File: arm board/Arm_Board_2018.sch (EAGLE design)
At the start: 212 parts, among them J1 RJ45KEYSTONE-942, J10 APP_2POS_CONFIGGENERAL_CONFIG, J11 APP_2POS_CONFIGGENERAL_CONFIG, J12 APP_2POS_CONFIGGENERAL_CONFIG, J13 APP_2POS_CONFIGGENERAL_CONFIG, J14 SL02, J15 SL02, J16 SL02, J2 JTAG_ARM_10PIN, J4 SL02, J5 APP_2POS_CONFIGGENERAL_CONFIG, J6 APP_2POS_CONFIGGENERAL_CONFIG, J7 APP_2POS_CONFIGGENERAL_CONFIG, J9 APP_2POS_CONFIGGENERAL_CONFIG, Q1 Q_IRF7437SMD, U1 TM4C1294NCPDT, U2 HX1198FNL, U3 SLVU2.8-4, Y1 NX3225GA, Y2 CRYATL_32K_SMD

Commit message: Attached most of the powerlines
All major components put on the board. Most powerlines have been run.
Started to route a logic bus.
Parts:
- removed R60, R67, R68, R69, R70: 1k, SparkFun-Passives:RESISTOR0402-RES
- C50: device SparkFun-Capacitors:CAP1206 -> SparkFun-Passives:CAP0603-CAP
- C51: value 2.2uF -> 10nF; device SparkFun-Capacitors:CAP1206 -> SparkFun-Passives:CAP0603-CAP
- C61: value .1uF -> 2.2uF; device SparkFun-Passives:CAP0603-CAP -> SparkFun-Passives:CAP1206
- C62: value 1nF -> 2.2uF; device SparkFun-Passives:CAP0603-CAP -> SparkFun-Passives:CAP1206
- C63, C65, C67: value .1uF -> 0.1uF
- C64, C66, C68: value .1uF -> 10nF
- C69, C71, C73, C74: value 1uF -> 0.1uF
- C70, C72: value 1uF -> 10nF
- C75: value 2.2uF -> 1nF; device SparkFun-Capacitors:CAP1206 -> SparkFun-Passives:CAP0603-CAP
- R59: value 1k -> 1K
- U$21, U$22, U$23, U$24, U$25: value ACS781 -> ACS722LL; device MRDT-ICs:ACS781 -> MRDT-ICs:ACS722LL
- renumbered GND97 to POWER_12V2
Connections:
- removed net N$13: R60.1, U$25.VOUT
- removed net N$14: C53.2, Q1.D, U$19.SENSE, U$19.V+, U$26.IP-
- removed net N$2: R30.2, R31.2, U$12.VREF
- removed net N$26: R35.2, R36.2, U$13.VREF
- removed net N$3: C55.2, R18.2, R20.1, U$14.I0, U$14.I1, U$14.I2, U$14.I3, U$14.I4, U$14.NSLEEP, U$14.V3P3OUT
- removed net N$4: R40.2, R41.2, U$15.VREF
- removed net N$44: R70.1, U$20.VOUT
- new net N$100: R59.2, U$20.VOUT
- new net N$48: C53.2, Q1.D, U$19.SENSE, U$19.V+, U$20.IP-
- new net N$52: C65.2, U$21.SEL, U$21.VCC
- new net N$76: C64.2, U$21.VIOUT
- new net N$78: C67.2, U$22.SEL, U$22.VCC
- new net N$82: C66.2, U$22.VIOUT
- new net N$83: C69.2, U$24.SEL, U$24.VCC
- new net N$84: C68.2, U$24.VIOUT
- new net N$85: C71.2, U$26.SEL, U$26.VCC
- new net N$86: C70.2, U$26.VIOUT
- new net N$87: C73.2, U$25.SEL, U$25.VCC
- new net N$96: C72.2, U$25.VIOUT
- new net N$98: C63.2, U$23.SEL, U$23.VCC
- new net N$99: C51.2, U$23.VIOUT
- net 12VMOTOR_POWER: now also U$26.IP+; no longer U$20.IP+
- net GND: now also C61.1, C74.2; no longer C51.1, C61.2, C63.1, C64.1, C65.1, C66.1, C67.1, C68.1, C69.2, C70.2, C71.1, C72.1, C73.1, C74.1
- net LOGIC_3.3V: now also C50.1, C63.1, C65.1, C67.1, C69.1, C71.1, C73.1, C74.1; no longer C61.1, C63.2, C64.2, C65.2, C66.2, C67.2, C68.2, C75.1, U$21.VCC, U$22.VCC, U$23.VCC, U$24.VCC, U$25.VCC, U$26.SEL, U$26.VCC
- net MAINLINE_CURRENT_SENSOR: now also C75.1, R59.1; no longer C62.2, U$26.VIOUT
- net MOTOR1_CURRENT_SENSOR: now also C64.1; no longer C74.2, R70.2
- net MOTOR1_POWER: now also U$21.IP-; no longer U$20.IP-
- net MOTOR2_CURRENT_SENSOR: now also C66.1; no longer C73.2, R69.2
- net MOTOR3_CURRENT_SENSOR: now also C51.1; no longer C72.2, R68.2
- net MOTOR3_POWER: now also U$23.IP-; no longer U$21.IP-
- net MOTOR4_CURRENT_SENSOR: now also C68.1; no longer C71.2, R67.2
- net MOTOR4_POWER: now also U$24.IP-; no longer U$23.IP-
- net MOTOR5_CURRENT_SENSOR: now also C72.1; no longer C69.1, R59.2
- net MOTOR5_POWER: now also U$25.IP-; no longer U$24.IP-
- net MOTOR6_CURRENT_SENSOR: no longer R60.2
- net MOTOR6_POWER: now also U$26.IP-; no longer U$25.IP-
- net N$1: now also C55.2, R18.2, R20.2, U$14.I0, U$14.I1, U$14.I2, U$14.I3, U$14.I4, U$14.NSLEEP, U$14.V3P3OUT; no longer R25.2, R26.2, U$11.VREF
- net N$12: now also R20.1, R21.2, U$14.VREF; no longer R59.1, U$24.VOUT
- net N$15: now also R35.1, R36.2, U$13.VREF; no longer C57.2, R24.2, R25.1, U$11.I0, U$11.I1, U$11.I2, U$11.I3, U$11.I4, U$11.NSLEEP, U$11.V3P3OUT
- net N$20: now also C57.2, R24.2, R25.2, U$11.I0, U$11.I1, U$11.I2, U$11.I3, U$11.I4, U$11.NSLEEP, U$11.V3P3OUT; no longer R67.1, U$23.VOUT
- net N$21: now also R45.1, R46.2, U$16.VREF; no longer C56.2, R29.2, R30.1, U$12.I0, U$12.I1, U$12.I2, U$12.I3, U$12.I4, U$12.NSLEEP, U$12.V3P3OUT
- net N$27: now also R40.1, R41.2, U$15.VREF; no longer C58.2, R34.2, R35.1, U$13.I0, U$13.I1, U$13.I2, U$13.I3, U$13.I4, U$13.NSLEEP, U$13.V3P3OUT
- net N$32: now also C59.2, R39.2, R40.2, U$15.I0, U$15.I1, U$15.I2, U$15.I3, U$15.I4, U$15.NSLEEP, U$15.V3P3OUT; no longer R68.1, U$21.VOUT
- net N$33: now also C60.2, R44.2, R45.2, U$16.I0, U$16.I1, U$16.I2, U$16.I3, U$16.I4, U$16.NSLEEP, U$16.V3P3OUT; no longer C59.2, R39.2, R40.1, U$15.I0, U$15.I1, U$15.I2, U$15.I3, U$15.I4, U$15.NSLEEP, U$15.V3P3OUT
- net N$38: now also C56.2, R29.2, R30.2, U$12.I0, U$12.I1, U$12.I2, U$12.I3, U$12.I4, U$12.NSLEEP, U$12.V3P3OUT; no longer R69.1, U$22.VOUT
- net N$39: now also C58.2, R34.2, R35.2, U$13.I0, U$13.I1, U$13.I2, U$13.I3, U$13.I4, U$13.NSLEEP, U$13.V3P3OUT; no longer C60.2, R44.2, R45.1, U$16.I0, U$16.I1, U$16.I2, U$16.I3, U$16.I4, U$16.NSLEEP, U$16.V3P3OUT
- net N$5: now also R30.1, R31.2, U$12.VREF; no longer R45.2, R46.2, U$16.VREF
- net N$6: now also R25.1, R26.2, U$11.VREF; no longer R20.2, R21.2, U$14.VREF
- net VCC_12V: now also C61.2, C62.2, U$20.IP+; no longer C50.1, C51.2, U$26.IP+
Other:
- note added: "BOARD LEDS"
- note added: "MAIN POWER LINE"
- note removed: "MAIN POWER INPUT"
- note removed: "MOTOR MANUAL CONTROL LEDS"
- moved on the sheet: C21, C23, C25, C26, C29, C30, C33, C34, C37, C38, C41, C42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

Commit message: Add all pins, finished Rev 1, Not board reviewed
Added all the pins that were missing. Finished routing all logic lines.
Made board slightly smaller.
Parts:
- removed C24, C25, C28, C29, C32, C33, C36, C37, C40, C41, C48, C49, C54: .1uF, SparkFun-Passives:CAP0603-CAP
- removed C26, C30, C34, C38, C42: 100uF, SparkFun-Passives:CAP1210
- removed C27, C31, C35, C39, C43: .01uF, SparkFun-Passives:CAP0603-CAP
- removed C55, C56, C57, C58, C59, C60: .47uF, SparkFun-Passives:CAP0603-CAP
- removed R21, R24, R26, R29, R31, R34, R36, R39, R41, R44, R46: 10K, SparkFun-Passives:RESISTOR0402-RES
- removed R22, R27, R32, R37, R42, R47: 40m, SparkFun-Passives:RESISTOR2512
- removed R23, R28, R33, R38, R43, R48: 1m, SparkFun-Passives:RESISTOR0402-RES
- removed R25, R30, R35, R40, R45: 22.6K, SparkFun-Passives:RESISTOR0402-RES
- removed U$13, U$14, U$15, U$16: DRV8829, MRDT-ICs:DRV8829
- removed U$18, U$27, U$28: 74LVC1G3157, MRDT-ICs:74LVC1G3157
- added C76, C78, C80, C82: .1uF, SparkFun-Passives:CAP0603-CAP
- added C77, C79, C81, C83: 100uF, SparkFun-Passives:CAP1210
- added GROUND: APPPP45_PCB_HORIZ_RIGHT, MRDT-Connectors:APPPP45_PCB_HORIZ_RIGHT
- added OE_PULLUP, R60, R67, R68, R69: 10K, SparkFun-Passives:RESISTOR0402-RES
- added SCL_PULLUP, SDA_PULLUP: 1K, SparkFun-Passives:RESISTOR0402-RES
- added U$31, U$32, U$33, U$34: BTM7752G, MRDT-ICs:BTM7752G
- added U4: (no value), adafruit:PCA9685
- C21: value .1uF -> 100uF; device SparkFun-Passives:CAP0603-CAP -> SparkFun-Passives:CAP1210
- C22: value .01uF -> .1uF
- D1: value (none) -> J1
- D2: value (none) -> J2
- D3: value (none) -> J3
- D4: value (none) -> J4
- D5: value (none) -> J5
- D6: value (none) -> J6
- R20: value 22.6K -> 10K
- U$11, U$12: value DRV8829 -> BTM7752G; device MRDT-ICs:DRV8829 -> MRDT-ICs:BTM7752G
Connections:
- removed net MOTOR1_DEMUX_SEL: U$27.Z, U1G$1.PD3@4
- removed net MOTOR1_GEN0: U$27.S, U1G$1.PF1@43
- removed net MOTOR2_GEN1: U$14.ENABLE, U1G$1.PF2@44
- removed net MOTOR2_NFAULT: R18.1, U$14.NFAULT, U1G$1.PE0@15
- removed net MOTOR2_NRESET: U$14.NRESET, U1G$1.PE1@14
- removed net MOTOR2_PHASE: U$14.PHASE, U1G$1.PE2@13
- removed net MOTOR3_DEMUX_SEL: U$18.Z, U1G$1.PD5@126
- removed net MOTOR3_GEN1: U$18.S, U1G$1.PF3@45
- removed net MOTOR4_GEN2: U$11.ENABLE, U1G$1.PG0@49
- removed net MOTOR4_NFAULT: R24.1, U$11.NFAULT, U1G$1.PE3@12
- removed net MOTOR4_NRESET: U$11.NRESET, U1G$1.PE4@123
- removed net MOTOR4_PHASE: U$11.PHASE, U1G$1.PE5@124
- removed net MOTOR5_GEN2: U$12.ENABLE, U1G$1.PG1@50
- removed net MOTOR5_NFAULT: R29.1, U$12.NFAULT, U1G$1.PC4@25
- removed net MOTOR5_NRESET: U$12.NRESET, U1G$1.PC5@24
- removed net MOTOR5_PHASE: U$12.PHASE, U1G$1.PC6@23
- removed net MOTOR6_GEN3: U$13.ENABLE, U1G$1.PK4@63
- removed net MOTOR6_NFAULT: R34.1, U$13.NFAULT, U1G$1.PN2@109
- removed net MOTOR6_NRESET: U$13.NRESET, U1G$1.PN3@110
- removed net MOTOR6_PHASE: U$13.PHASE, U1G$1.PN4@111
- removed net MOTOR7/8_DEMUX_SEL: U$28.Z, U1G$1.PD7@128
- removed net MOTOR7/8_GEN3: U$28.S, U1G$1.PK5@62
- removed net MOTOR7_NFAULT: R39.1, U$15.NFAULT, U1G$1.PQ1@6
- removed net MOTOR7_NRESET: U$15.NRESET, U1G$1.PQ2@11
- removed net MOTOR7_PHASE: U$15.PHASE, U1G$1.PQ3@27
- removed net MOTOR7_PWM: U$15.ENABLE, U$28.Y1
- removed net MOTOR8_NFAULT: R44.1, U$16.NFAULT, U1G$1.PQ0@5
- removed net MOTOR8_NRESET: U$16.NRESET, U1G$1.PP0@118
- removed net MOTOR8_PHASE: U$16.PHASE, U1G$1.PP1@119
- removed net MOTOR8_PWM: U$16.ENABLE, U$28.Y0
- removed net N$1: C55.2, R18.2, R20.2, U$14.I0, U$14.I1, U$14.I2, U$14.I3, U$14.I4, U$14.NSLEEP, U$14.V3P3OUT
- removed net N$10: C22.1, U$14.CP1
- removed net N$11: C22.2, U$14.CP2
- removed net N$12: R20.1, R21.2, U$14.VREF
- removed net N$15: R35.1, R36.2, U$13.VREF
- removed net N$16: R27.1, U$11.ISENSE
- removed net N$17: C24.1, R28.1, U$11.VCP
- removed net N$18: C27.1, U$11.CP1
- removed net N$19: C27.2, U$11.CP2
- removed net N$20: C57.2, R24.2, R25.2, U$11.I0, U$11.I1, U$11.I2, U$11.I3, U$11.I4, U$11.NSLEEP, U$11.V3P3OUT
- removed net N$21: R45.1, R46.2, U$16.VREF
- removed net N$22: R32.1, U$12.ISENSE
- removed net N$23: C28.1, R33.1, U$12.VCP
- removed net N$24: C31.1, U$12.CP1
- removed net N$25: C31.2, U$12.CP2
- removed net N$27: R40.1, R41.2, U$15.VREF
- removed net N$28: R37.1, U$13.ISENSE
- removed net N$29: C32.1, R38.1, U$13.VCP
- removed net N$30: C35.1, U$13.CP1
- removed net N$31: C35.2, U$13.CP2
- removed net N$32: C59.2, R39.2, R40.2, U$15.I0, U$15.I1, U$15.I2, U$15.I3, U$15.I4, U$15.NSLEEP, U$15.V3P3OUT
- removed net N$33: C60.2, R44.2, R45.2, U$16.I0, U$16.I1, U$16.I2, U$16.I3, U$16.I4, U$16.NSLEEP, U$16.V3P3OUT
- removed net N$34: R42.1, U$15.ISENSE
- removed net N$35: C36.1, R43.1, U$15.VCP
- removed net N$36: C39.1, U$15.CP1
- removed net N$37: C39.2, U$15.CP2
- removed net N$38: C56.2, R29.2, R30.2, U$12.I0, U$12.I1, U$12.I2, U$12.I3, U$12.I4, U$12.NSLEEP, U$12.V3P3OUT
- removed net N$39: C58.2, R34.2, R35.2, U$13.I0, U$13.I1, U$13.I2, U$13.I3, U$13.I4, U$13.NSLEEP, U$13.V3P3OUT
- removed net N$40: R47.1, U$16.ISENSE
- removed net N$41: C40.1, R48.1, U$16.VCP
- removed net N$42: C43.1, U$16.CP1
- removed net N$43: C43.2, U$16.CP2
- removed net N$7: R22.1, U$14.ISENSE
- removed net N$8: C20.1, R23.1, U$14.VCP
- new net MOTOR2_ENABLE: U$34.INH, U1G$1.PN3@110
- new net MOTOR2_PWM1: U$34.IN1, U4.PWM2
- new net MOTOR2_PWM2: U$34.IN2, U4.PWM3
- new net MOTOR4_ENABLE: U$11.INH, U1G$1.PJ0@116
- new net MOTOR4_PWM1: U$11.IN1, U4.PWM6
- new net MOTOR4_PWM2: U$11.IN2, U4.PWM7
- new net MOTOR5_ENABLE: U$33.INH, U1G$1.PJ1@117
- new net MOTOR5_PWM1: U$33.IN1, U4.PWM8
- new net MOTOR5_PWM2: U$33.IN2, U4.PWM9
- new net MOTOR6_ENABLE: U$31.INH, U1G$1.PP0@118
- new net MOTOR6_PWM1: U$31.IN1, U4.PWM10
- new net MOTOR6_PWM2: U$31.IN2, U4.PWM11
- new net MOTOR7_ENABLE: U$17.INH, U1G$1.PP1@119
- new net MOTOR7_PWM1: U$17.IN1, U4.PWM12
- new net MOTOR7_PWM2: U$17.IN2, U4.PWM13
- new net MOTOR8_ENABLE: U$29.INH, U1G$1.PB5@120
- new net MOTOR8_PWM1: U$29.IN1, U4.PWM14
- new net MOTOR8_PWM2: U$29.IN2, U4.PWM15
- new net N$44: R60.2, U$31.IS
- new net N$46: R67.2, U$32.IS
- new net N$50: R68.2, U$33.IS
- new net N$51: R69.2, U$34.IS
- new net PWM_ADDRESS_BIT_A0: U1G$1.PE3@12, U4.A0
- new net PWM_ADDRESS_BIT_A1: U1G$1.PQ2@11, U4.A1
- new net PWM_ADDRESS_BIT_A2: U1G$1.PQ1@6, U4.A2
- new net PWM_ADDRESS_BIT_A3: U1G$1.PQ0@5, U4.A3
- new net PWM_ADDRESS_BIT_A4: U1G$1.PD3@4, U4.A4
- new net PWM_ADDRESS_BIT_A5: U1G$1.PE2@13, U4.A5
- new net PWM_DRIVER_SCL: SCL_PULLUP.2, U1G$1.PN5@112, U4.SCL
- new net PWM_DRIVER_SDA: SDA_PULLUP.2, U1G$1.PN4@111, U4.SDA
- new net PWM_OUTPUT_ENABLE: OE_PULLUP.2, U1G$1.PE1@14, U4.#OE
- net 12VMOTOR_POWER: now also C44.2, C45.2, C46.2, C47.2, U$17.VS, U$29.VS; no longer C36.2, C37.2, C38.2, C40.2, C41.2, C42.2, R43.2, R48.2, U$15.VM, U$16.VM
- net BUTTON1: now also U1G$1.PC5@24; no longer U1G$1.PL0@81
- net BUTTON2: now also U1G$1.PC4@25; no longer U1G$1.PL1@82
- net BUTTON3: now also U1G$1.PQ3@27; no longer U1G$1.PL2@83
- net GND: now also C20.1, C22.1, C76.1, C77.1, C78.1, C79.1, C80.1, C81.1, C82.1, C83.1, GROUND.P$1, R18.1, R20.1, R60.1, R67.1, R68.1, R69.1, U$31.GND, U$32.GND, U$33.GND, U$34.GND, U4.EXTCLK, U4.GND; no longer C25.1, C26.1, C29.1, C30.1, C33.1, C34.1, C37.1, C38.1, C41.1, C42.1, C48.1, C49.1, C54.1, C55.1, C56.1, C57.1, C58.1, C59.1, C60.1, R21.1, R22.2, R26.1, R27.2, R31.1, R32.2, R36.1, R37.2, R41.1, R42.2, R46.1, R47.2, U$13.GND, U$14.GND, U$15.GND, U$16.GND, U$18.GND, U$27.GND, U$28.GND
- net LED1: now also U1G$1.PC6@23; no longer U1G$1.PA4@37
- net LED2: now also U1G$1.PC7@22; no longer U1G$1.PA5@38
- net LED3: now also U1G$1.PK3@21; no longer U1G$1.PB2@91
- net LED4: now also U1G$1.PK2@20; no longer U1G$1.PB3@92
- net LED5: now also U1G$1.PK1@19; no longer U1G$1.PC7@22
- net LED6: now also U1G$1.PK0@18; no longer U1G$1.PD1@2
- net LIMIT_SWITCH_1: now also U1G$1.PH3@32; no longer U1G$1.PH0@29
- net LIMIT_SWITCH_2: now also U1G$1.PH2@31; no longer U1G$1.PH1@30
- net LIMIT_SWITCH_3: now also U1G$1.PH1@30; no longer U1G$1.PK6@61
- net LOGIC_3.3V: now also OE_PULLUP.1, SCL_PULLUP.1, SDA_PULLUP.1, U4.VDD; no longer C48.2, C49.2, C54.2, U$18.VCC, U$27.VCC, U$28.VCC
- net MAINLINE_CURRENT_SENSOR: now also U1G$1.PB4@121; no longer U1G$1.PD0@1
- net MASTER_POWER_ENABLE: now also U1G$1.PN2@109; no longer U1G$1.PL4@85
- net MOTOR1_1: now also U$12.OUT1; no longer U$17.OUT1
- net MOTOR1_2: now also U$12.OUT2; no longer U$17.OUT2
- net MOTOR1_CURRENT_SENSOR: now also U1G$1.PE4@123; no longer U1G$1.PB4@121
- net MOTOR1_ENABLE: now also U$12.INH, U1G$1.PB1@96; no longer U$17.INH, U1G$1.PM5@73
- net MOTOR1_POWER: now also C22.2, C23.2, U$12.VS; no longer C44.2, C45.2, U$17.VS
- net MOTOR1_PWM1: now also U$12.IN1, U4.PWM0; no longer U$17.IN1, U$27.Y1
- net MOTOR1_PWM2: now also U$12.IN2, U4.PWM1; no longer U$17.IN2, U$27.Y0
- net MOTOR2_1: now also U$34.OUT1; no longer U$14.OUT1
- net MOTOR2_2: now also U$34.OUT2; no longer U$14.OUT2
- net MOTOR2_CURRENT_SENSOR: now also U1G$1.PE5@124; no longer U1G$1.PB5@120
- net MOTOR2_POWER: now also C82.2, C83.2, U$34.VS; no longer C20.2, C21.2, C23.2, R23.2, U$14.VM
- net MOTOR3_1: now also U$32.OUT1; no longer U$29.OUT1
- net MOTOR3_2: now also U$32.OUT2; no longer U$29.OUT2
- net MOTOR3_CURRENT_SENSOR: now also U1G$1.PD5@126; no longer U1G$1.PK0@18
- net MOTOR3_ENABLE: now also U$32.INH, U1G$1.PE0@15; no longer U$29.INH, U1G$1.PM7@71
- net MOTOR3_POWER: now also C78.2, C79.2, U$32.VS; no longer C46.2, C47.2, U$29.VS
- net MOTOR3_PWM1: now also U$32.IN1, U4.PWM4; no longer U$18.Y1, U$29.IN1
- net MOTOR3_PWM2: now also U$32.IN2, U4.PWM5; no longer U$18.Y0, U$29.IN2
- net MOTOR4_CURRENT_SENSOR: now also U1G$1.PD6@127; no longer U1G$1.PK1@19
- net MOTOR4_POWER: now also C20.2, C21.2, U$11.VS; no longer C24.2, C25.2, C26.2, R28.2, U$11.VM
- net MOTOR5_1: now also U$33.OUT1; no longer U$12.OUT1
- net MOTOR5_2: now also U$33.OUT2; no longer U$12.OUT2
- net MOTOR5_CURRENT_SENSOR: now also U1G$1.PD0@1; no longer U1G$1.PK2@20
- net MOTOR5_POWER: now also C80.2, C81.2, U$33.VS; no longer C28.2, C29.2, C30.2, R33.2, U$12.VM
- net MOTOR6_1: now also U$31.OUT1; no longer U$13.OUT1
- net MOTOR6_2: now also U$31.OUT2; no longer U$13.OUT2
- net MOTOR6_CURRENT_SENSOR: now also U1G$1.PD1@2; no longer U1G$1.PK3@21
- net MOTOR6_POWER: now also C76.2, C77.2, U$31.VS; no longer C32.2, C33.2, C34.2, R38.2, U$13.VM
- net MOTOR7_1: now also U$17.OUT1; no longer U$15.OUT1
- net MOTOR7_2: now also U$17.OUT2; no longer U$15.OUT2
- net MOTOR8_1: now also U$29.OUT1; no longer U$16.OUT1
- net MOTOR8_2: now also U$29.OUT2; no longer U$16.OUT2
- net N$5: now also R18.2, U$11.IS; no longer R30.1, R31.2, U$12.VREF
- net N$6: now also R20.2, U$12.IS; no longer R25.1, R26.2, U$11.VREF
- net SWITCH: now also U1G$1.PH0@29; no longer U1G$1.PL3@84

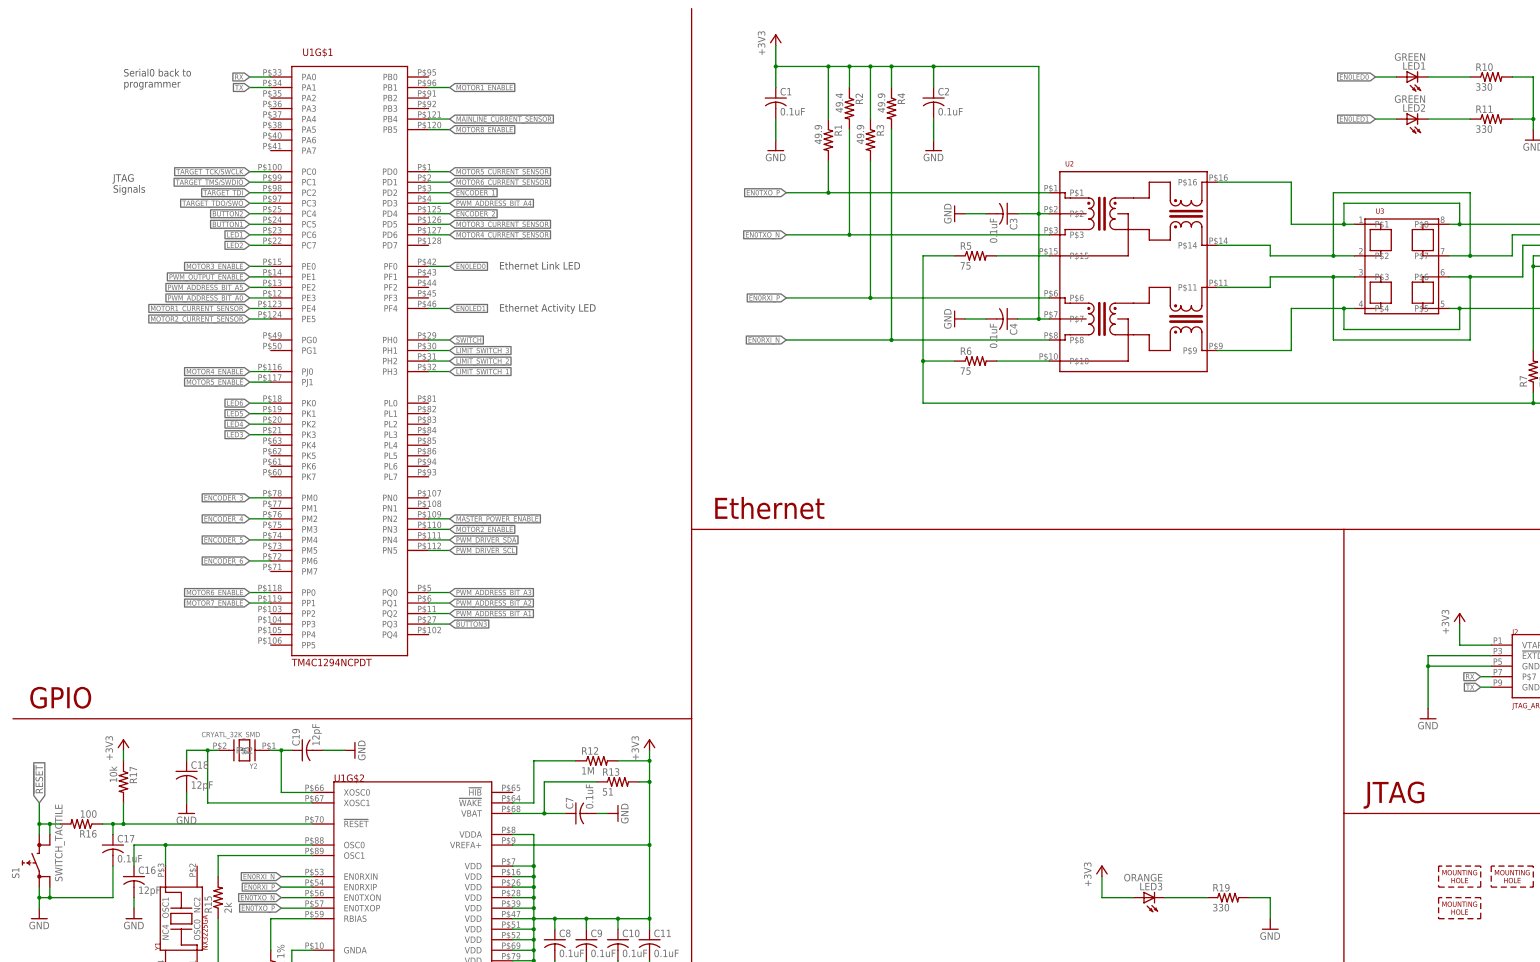
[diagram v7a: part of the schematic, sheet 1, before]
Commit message: Connected the 3V3 plane to Logic 3.3V input
Fixed the fact that the tiva would not have any power without connecting
to the logic line.
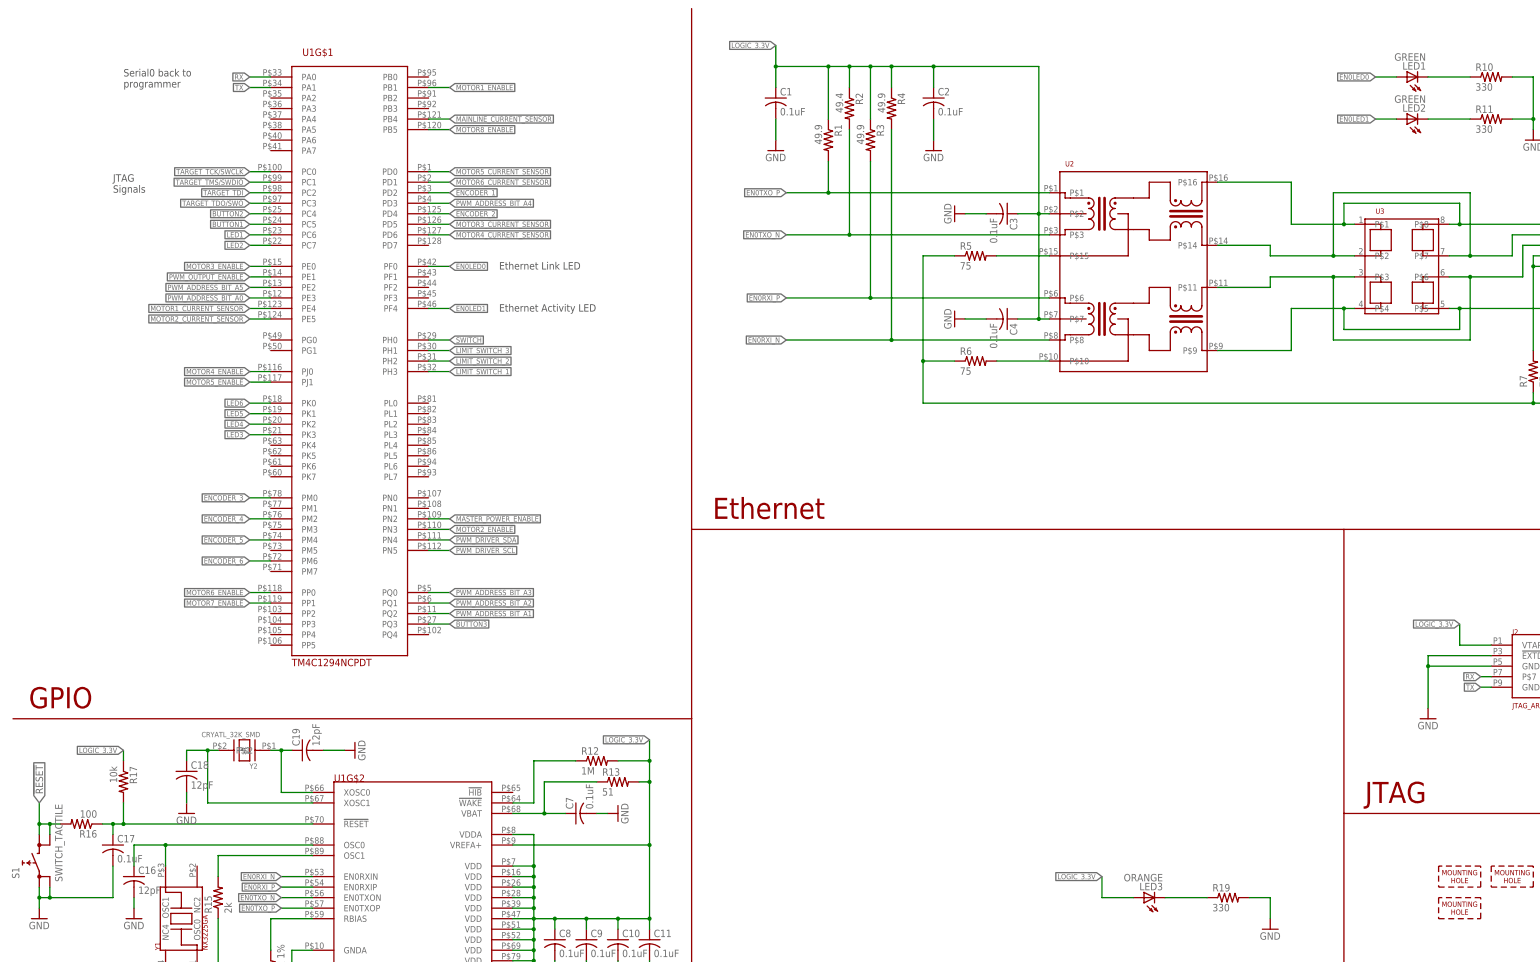
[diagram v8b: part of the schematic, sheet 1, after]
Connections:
- removed net +3V3: C1.1, C10.1, C11.1, C2.1, C3.1, C4.1, C8.1, C9.1, J2.VTARGET, LED3.A, R1.1, R12.2, R13.2, R17.1, R2.1, R3.1, R4.1, U1G$2.VDD@101, U1G$2.VDD@113, U1G$2.VDD@122, U1G$2.VDD@16, U1G$2.VDD@26, U1G$2.VDD@28, U1G$2.VDD@39, U1G$2.VDD@47, U1G$2.VDD@51, U1G$2.VDD@52, U1G$2.VDD@69, U1G$2.VDD@7, U1G$2.VDD@79, U1G$2.VDD@90, U1G$2.VDDA@8, U1G$2.VREFA+@9, U2.P$2, U2.P$7
- net LOGIC_3.3V: now also C1.1, C10.1, C11.1, C2.1, C3.1, C4.1, C8.1, C9.1, J2.VTARGET, LED3.A, R1.1, R12.2, R13.2, R17.1, R2.1, R3.1, R4.1, U1G$2.VDD@101, U1G$2.VDD@113, U1G$2.VDD@122, U1G$2.VDD@16, U1G$2.VDD@26, U1G$2.VDD@28, U1G$2.VDD@39, U1G$2.VDD@47, U1G$2.VDD@51, U1G$2.VDD@52, U1G$2.VDD@69, U1G$2.VDD@7, U1G$2.VDD@79, U1G$2.VDD@90, U1G$2.VDDA@8, U1G$2.VREFA+@9, U2.P$2, U2.P$7
